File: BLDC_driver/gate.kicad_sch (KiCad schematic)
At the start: 9 parts, among them Q1 AOTL66912, Q2 AOTL66912, Q3 AOTL66912

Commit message: Layout progress
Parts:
- removed R34, R35, R36: 2R2, Resistor_SMD:R_0603_1608Metric, symbol Device:R_Small
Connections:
- net G: now also C20.1, C21.1, C22.1, Q1.1 (G), Q2.1 (G), Q3.1 (G)

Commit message: Layout progress
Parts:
- renumbered C20 to C24, C21 to C25, C22 to C26
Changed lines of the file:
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@@
 		(on_board yes)
 		(dnp no)
-		(property "Reference" "C20"
+		(property "Reference" "C24"
 			(at 117.602 62.738 0)
 			(effects
@@
 			(project "BLDC_driver"
 				(path "/6f399879-dc45-4210-87b6-ea005f89c132/156cc71e-604a-4062-8209-9f4827fd9816/1e0673b2-28ee-4abd-8d95-4b0ef315a2ba"
-					(reference "C32")
+					(reference "C36")
 					(unit 1)
 				)
 				(path "/6f399879-dc45-4210-87b6-ea005f89c132/156cc71e-604a-4062-8209-9f4827fd9816/3b5a2433-0d94-4db3-8acf-77e522752851"
-					(reference "C26")
+					(reference "C30")
 					(unit 1)
 				)
 				(path "/6f399879-dc45-4210-87b6-ea005f89c132/156cc71e-604a-4062-8209-9f4827fd9816/5d5b6445-583e-40c6-a8e8-a33863d8b053"
-					(reference "C29")
+					(reference "C33")
 					(unit 1)
 				)
 				(path "/6f399879-dc45-4210-87b6-ea005f89c132/156cc71e-604a-4062-8209-9f4827fd9816/6db2acd3-f369-4a7f-afef-f4c39b70a001"
-					(reference "C35")
+					(reference "C39")
 					(unit 1)
 				)
 				(path "/6f399879-dc45-4210-87b6-ea005f89c132/156cc71e-604a-4062-8209-9f4827fd9816/c280de8f-0649-48b6-ad0a-7e5ac2423fd0"
-					(reference "C23")
+					(reference "C27")
 					(unit 1)
 				)
 				(path "/6f399879-dc45-4210-87b6-ea005f89c132/156cc71e-604a-4062-8209-9f4827fd9816/c5a9ed6b-6ba3-4697-827a-af8ff1c70cda"
-					(reference "C20")
+					(reference "C24")
 					(unit 1)
 				)
@@
 		(on_board yes)
 		(dnp no)
-		(property "Reference" "C21"
+		(property "Reference" "C25"
 			(at 143.002 62.738 0)
 			(effects
@@
 			(project "BLDC_driver"
 				(path "/6f399879-dc45-4210-87b6-ea005f89c132/156cc71e-604a-4062-8209-9f4827fd9816/1e0673b2-28ee-4abd-8d95-4b0ef315a2ba"
-					(reference "C33")
+					(reference "C37")
 					(unit 1)
 				)
 				(path "/6f399879-dc45-4210-87b6-ea005f89c132/156cc71e-604a-4062-8209-9f4827fd9816/3b5a2433-0d94-4db3-8acf-77e522752851"
-					(reference "C27")
+					(reference "C31")
 					(unit 1)
 				)
 				(path "/6f399879-dc45-4210-87b6-ea005f89c132/156cc71e-604a-4062-8209-9f4827fd9816/5d5b6445-583e-40c6-a8e8-a33863d8b053"
-					(reference "C30")
+					(reference "C34")
 					(unit 1)
 				)
 				(path "/6f399879-dc45-4210-87b6-ea005f89c132/156cc71e-604a-4062-8209-9f4827fd9816/6db2acd3-f369-4a7f-afef-f4c39b70a001"
-					(reference "C36")
+					(reference "C40")
 					(unit 1)
 				)
 				(path "/6f399879-dc45-4210-87b6-ea005f89c132/156cc71e-604a-4062-8209-9f4827fd9816/c280de8f-0649-48b6-ad0a-7e5ac2423fd0"
-					(reference "C24")
+					(reference "C28")
 					(unit 1)
 				)
 				(path "/6f399879-dc45-4210-87b6-ea005f89c132/156cc71e-604a-4062-8209-9f4827fd9816/c5a9ed6b-6ba3-4697-827a-af8ff1c70cda"
-					(reference "C21")
+					(reference "C25")
 					(unit 1)
 				)
@@
 		(on_board yes)
 		(dnp no)
-		(property "Reference" "C22"
+		(property "Reference" "C26"
 			(at 168.402 62.738 0)
 			(effects
@@
 			(project "BLDC_driver"
 				(path "/6f399879-dc45-4210-87b6-ea005f89c132/156cc71e-604a-4062-8209-9f4827fd9816/1e0673b2-28ee-4abd-8d95-4b0ef315a2ba"
-					(reference "C34")
+					(reference "C38")
 					(unit 1)
 				)
 				(path "/6f399879-dc45-4210-87b6-ea005f89c132/156cc71e-604a-4062-8209-9f4827fd9816/3b5a2433-0d94-4db3-8acf-77e522752851"
-					(reference "C28")
+					(reference "C32")
 					(unit 1)
 				)
 				(path "/6f399879-dc45-4210-87b6-ea005f89c132/156cc71e-604a-4062-8209-9f4827fd9816/5d5b6445-583e-40c6-a8e8-a33863d8b053"
-					(reference "C31")
+					(reference "C35")
 					(unit 1)
 				)
 				(path "/6f399879-dc45-4210-87b6-ea005f89c132/156cc71e-604a-4062-8209-9f4827fd9816/6db2acd3-f369-4a7f-afef-f4c39b70a001"
-					(reference "C37")
+					(reference "C41")
 					(unit 1)
 				)
 				(path "/6f399879-dc45-4210-87b6-ea005f89c132/156cc71e-604a-4062-8209-9f4827fd9816/c280de8f-0649-48b6-ad0a-7e5ac2423fd0"
-					(reference "C25")
+					(reference "C29")
 					(unit 1)
 				)
 				(path "/6f399879-dc45-4210-87b6-ea005f89c132/156cc71e-604a-4062-8209-9f4827fd9816/c5a9ed6b-6ba3-4697-827a-af8ff1c70cda"
-					(reference "C22")
-					(unit 1)
-				)
+					(reference "C26")
+					(unit 1)
+				)

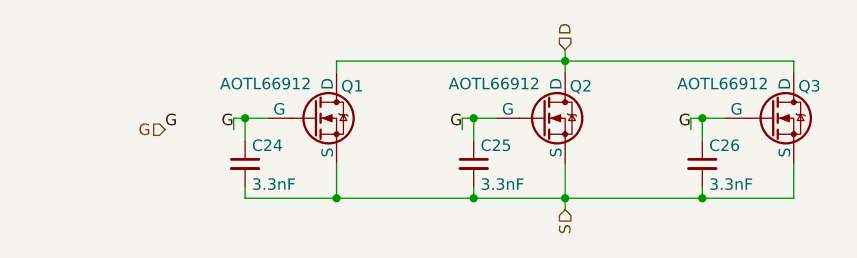
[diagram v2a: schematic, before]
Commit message: Started on power conversion section
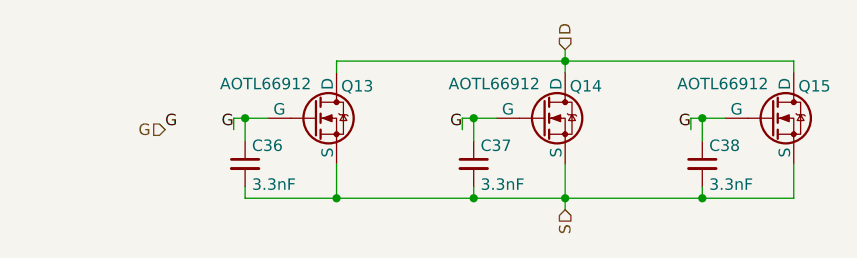
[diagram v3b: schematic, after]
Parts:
- renumbered C24 to C36, C25 to C37, C26 to C38, Q1 to Q13, Q2 to Q14, Q3 to Q15
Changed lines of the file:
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@@
 		(on_board yes)
 		(dnp no)
-		(property "Reference" "C24"
+		(property "Reference" "C36"
 			(at 117.602 62.738 0)
 			(effects
@@
 		(on_board yes)
 		(dnp no)
-		(property "Reference" "Q2"
+		(property "Reference" "Q14"
 			(at 152.908 56.134 0)
 			(effects
@@
 		(on_board yes)
 		(dnp no)
-		(property "Reference" "Q3"
+		(property "Reference" "Q15"
 			(at 178.308 56.134 0)
 			(effects
@@
 		(on_board yes)
 		(dnp no)
-		(property "Reference" "C25"
+		(property "Reference" "C37"
 			(at 143.002 62.738 0)
 			(effects
@@
 		(on_board yes)
 		(dnp no)
-		(property "Reference" "C26"
+		(property "Reference" "C38"
 			(at 168.402 62.738 0)
 			(effects
@@
 		(on_board yes)
 		(dnp no)
-		(property "Reference" "Q1"
+		(property "Reference" "Q13"
 			(at 127.508 56.134 0)
 			(effects
